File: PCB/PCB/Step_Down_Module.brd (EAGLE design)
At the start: 160 x 100 mm, 22 parts, among them Q1 TPH2900ENH

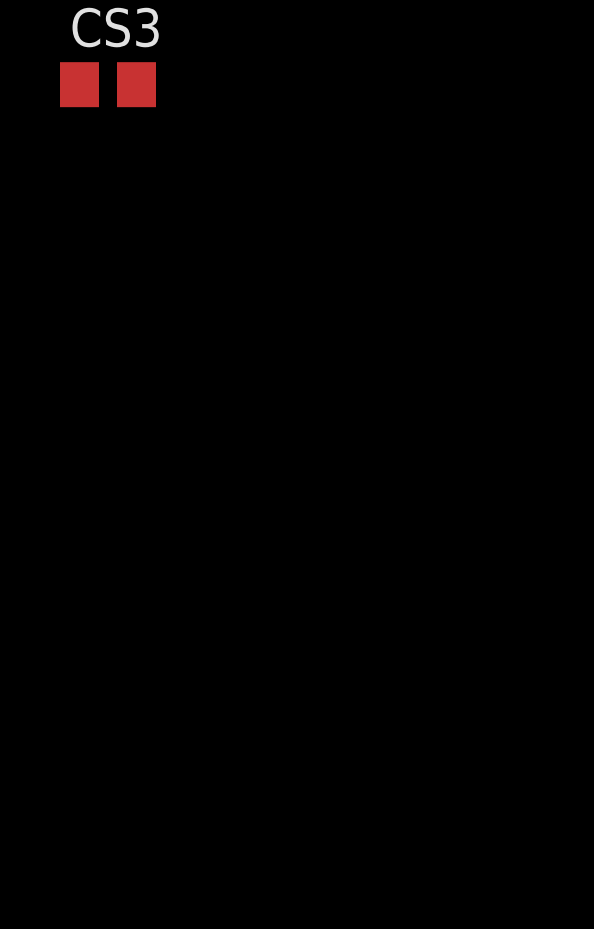
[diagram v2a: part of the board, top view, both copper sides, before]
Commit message: Working on schematic - Added I/O capacitors
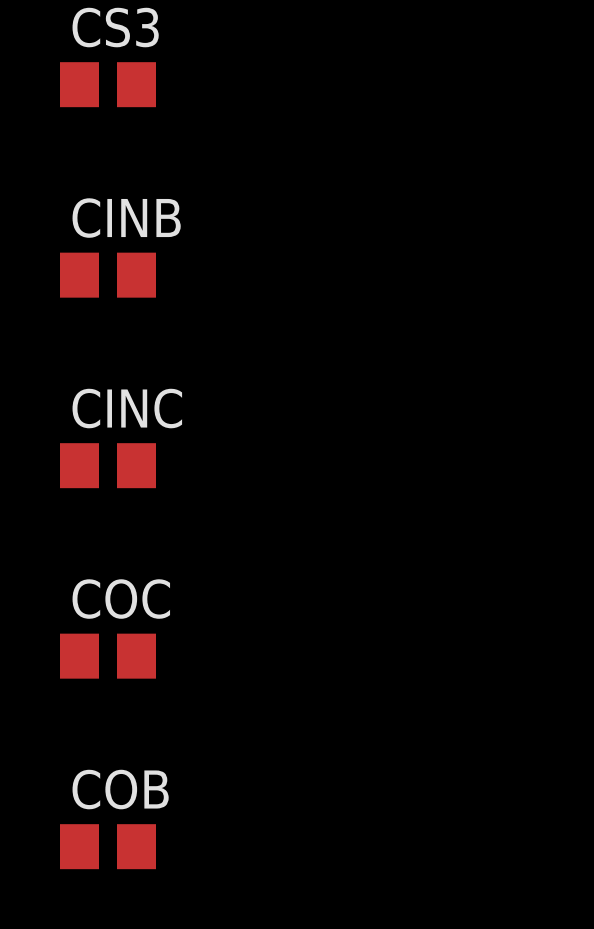
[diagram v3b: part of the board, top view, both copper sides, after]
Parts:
- added CINB: 47uF, rcl:C0805
- added CINC: .47uF, rcl:C0805
- added COB: 150uF, rcl:C0805
- added COC: 22uF, rcl:C0805
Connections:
- removed net N$5: CS.1, CS1.2, RFBT.2, RP.1, U$1.4, U$2.P1
- removed net N$9: U$1.30, U$1.34, U$3.D, U$3.D_1, U$3.D_2, U$3.D_3, U$3.D_4
- new net VIN: CINB.1, CINC.1, U$1.30, U$1.34, U$3.D, U$3.D_1, U$3.D_2, U$3.D_3, U$3.D_4
- new net VOUT: COB.1, COC.1, CS.1, CS1.2, RFBT.2, RP.1, U$1.4, U$2.P1
- net GND: now also CINB.2, CINC.2, COB.2, COC.2
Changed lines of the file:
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@@
 <attribute name="SPICEPREFIX" value="C" x="-35.56" y="-109.22" size="1.778" layer="27" display="off"/>
+</element>
+<element name="CINB" library="rcl" library_urn="urn:adsk.eagle:library:334" package="C0805" package3d_urn="urn:adsk.eagle:package:23617/2" value="47uF" x="-35.56" y="-115.57">
+<attribute name="SPICEPREFIX" value="C" x="-35.56" y="-115.57" size="1.778" layer="27" display="off"/>
+</element>
+<element name="CINC" library="rcl" library_urn="urn:adsk.eagle:library:334" package="C0805" package3d_urn="urn:adsk.eagle:package:23617/2" value=".47uF" x="-35.56" y="-121.92">
+<attribute name="SPICEPREFIX" value="C" x="-35.56" y="-121.92" size="1.778" layer="27" display="off"/>
+</element>
+<element name="COC" library="rcl" library_urn="urn:adsk.eagle:library:334" package="C0805" package3d_urn="urn:adsk.eagle:package:23617/2" value="22uF" x="-35.56" y="-128.27">
+<attribute name="SPICEPREFIX" value="C" x="-35.56" y="-128.27" size="1.778" layer="27" display="off"/>
+</element>
+<element name="COB" library="rcl" library_urn="urn:adsk.eagle:library:334" package="C0805" package3d_urn="urn:adsk.eagle:package:23617/2" value="150uF" x="-35.56" y="-134.62">
+<attribute name="SPICEPREFIX" value="C" x="-35.56" y="-134.62" size="1.778" layer="27" display="off"/>
 </element>
 </elements>
@@
 <wire x1="-36.51" y1="-6.35" x2="25.345" y2="28.48" width="0" layer="19" extent="1-1"/>
 </signal>
-<signal name="N$5">
+<signal name="VOUT">
 <contactref element="U$2" pad="P1"/>
 <contactref element="U$1" pad="4"/>
@@
 <contactref element="RFBT" pad="2"/>
 <contactref element="CS1" pad="2"/>
+<contactref element="COC" pad="1"/>
+<contactref element="COB" pad="1"/>
+<wire x1="-36.51" y1="-128.27" x2="-36.51" y2="-134.62" width="0" layer="19" extent="1-1"/>
+<wire x1="-34.61" y1="-39.37" x2="-36.51" y2="-128.27" width="0" layer="19" extent="1-1"/>
 <wire x1="-34.61" y1="-27.94" x2="-34.61" y2="-39.37" width="0" layer="19" extent="1-1"/>
 <wire x1="-36.51" y1="-21.59" x2="-34.61" y2="-27.94" width="0" layer="19" extent="1-1"/>
@@
 <wire x1="19.795" y1="33.98" x2="-36.51" y2="-27.94" width="0" layer="19" extent="1-1"/>
 </signal>
-<signal name="N$9">
+<signal name="VIN">
 <contactref element="U$1" pad="30"/>
 <contactref element="U$1" pad="34"/>
@@
 <contactref element="U$3" pad="D_1"/>
 <contactref element="U$3" pad="D_3"/>
-<wire x1="25.345" y1="32.48" x2="25.345" y2="34.48" width="0" layer="19" extent="1-1"/>
-<wire x1="-25.695" y1="-1.015" x2="25.345" y2="32.48" width="0" layer="19" extent="1-1"/>
-<wire x1="-26.345" y1="-1.015" x2="-25.695" y2="-1.015" width="0" layer="19" extent="1-1"/>
+<contactref element="CINB" pad="1"/>
+<contactref element="CINC" pad="1"/>
+<wire x1="-36.51" y1="-115.57" x2="-36.51" y2="-121.92" width="0" layer="19" extent="1-1"/>
+<wire x1="-26.67" y1="-2.09" x2="-36.51" y2="-115.57" width="0" layer="19" extent="1-1"/>
+<wire x1="-26.345" y1="-1.015" x2="-26.67" y2="-2.09" width="0" layer="19" extent="1-1"/>
+<wire x1="-25.695" y1="-1.015" x2="-26.345" y2="-1.015" width="0" layer="19" extent="1-1"/>
 <wire x1="-26.995" y1="-1.015" x2="-26.345" y2="-1.015" width="0" layer="19" extent="1-1"/>
 <wire x1="-27.645" y1="-1.015" x2="-26.995" y2="-1.015" width="0" layer="19" extent="1-1"/>
-<wire x1="-26.67" y1="-2.09" x2="-26.345" y2="-1.015" width="0" layer="19" extent="1-1"/>
+<wire x1="25.345" y1="32.48" x2="-25.695" y2="-1.015" width="0" layer="19" extent="1-1"/>
+<wire x1="25.345" y1="34.48" x2="25.345" y2="32.48" width="0" layer="19" extent="1-1"/>
 </signal>
 <signal name="N$10">
@@
 <contactref element="U$1" pad="36"/>
 <contactref element="CS3" pad="2"/>
+<contactref element="CINB" pad="2"/>
+<contactref element="CINC" pad="2"/>
+<contactref element="COC" pad="2"/>
+<contactref element="COB" pad="2"/>
+<wire x1="-34.61" y1="-128.27" x2="-34.61" y2="-134.62" width="0" layer="19" extent="1-1"/>
+<wire x1="-34.61" y1="-121.92" x2="-34.61" y2="-128.27" width="0" layer="19" extent="1-1"/>
+<wire x1="-34.61" y1="-115.57" x2="-34.61" y2="-121.92" width="0" layer="19" extent="1-1"/>
+<wire x1="-34.61" y1="-109.22" x2="-34.61" y2="-115.57" width="0" layer="19" extent="1-1"/>
 <wire x1="-36.51" y1="-83.82" x2="-34.61" y2="-109.22" width="0" layer="19" extent="1-1"/>
 <wire x1="-36.51" y1="-77.47" x2="-36.51" y2="-83.82" width="0" layer="19" extent="1-1"/>

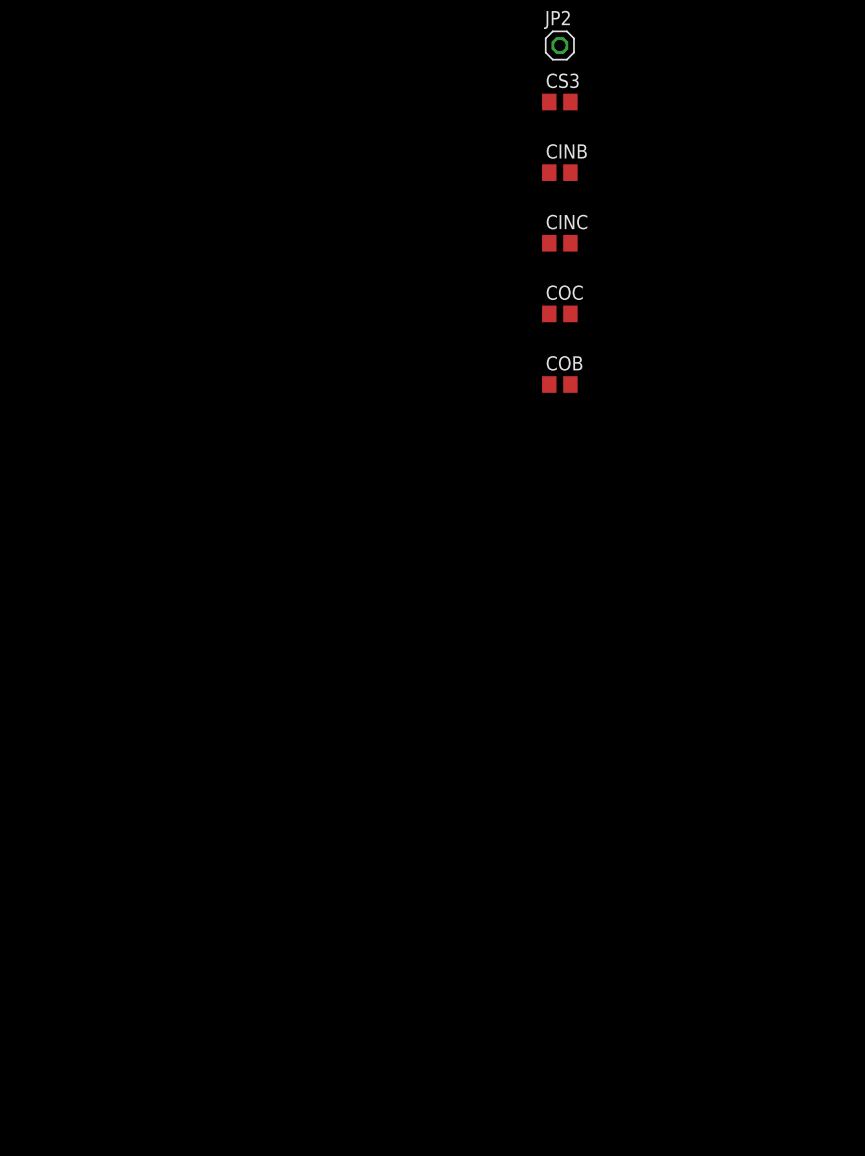
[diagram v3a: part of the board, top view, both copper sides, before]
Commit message: Working on schematic - Added DRVCC transistor, made a lot of changes to the pin state
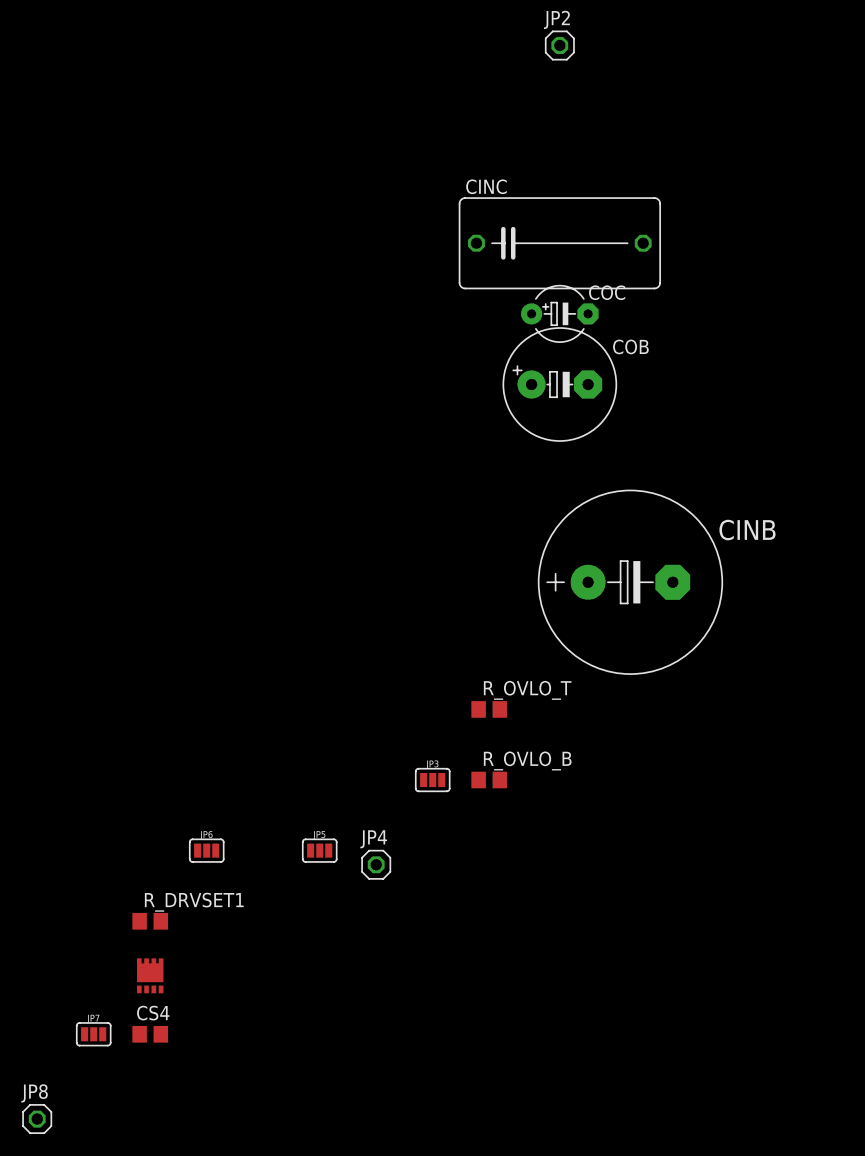
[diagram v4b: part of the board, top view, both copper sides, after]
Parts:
- removed CS3: 4.7uF, rcl:C0805
- added CS4: 4.7uF, rcl:C0805
- added JP3, JP5, JP6, JP7: JUMPER-SMT_3_1-NC_PASTE_SILK, SparkFun-Jumpers:SMT-JUMPER_3_1-NC_PASTE_SILK
- added JP4, JP8: (no value), pinhead:1X01
- added R_DRVSET1: 80.6k, rcl:R0805
- added R_OVLO_B: 1k, rcl:R0805
- added R_OVLO_T: 124k, rcl:R0805
- added U$4: FDMC86240, Switching_MOS:8-MLP/POWERWFDN
- CINB: device rcl:C0805 -> rcl:E7,5-16
- CINC: device rcl:C0805 -> rcl:C150-084X183
- COB: device rcl:C0805 -> rcl:E5-10,5
- COC: device rcl:C0805 -> rcl:E5-5
- moved CINB 37.4 mm to (-29.2, -152.4)
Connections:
- removed net N$14: CS3.1, U$1.26, U$1.28
- new net DRVCC: CS4.1, U$1.26, U$4.S_1, U$4.S_2, U$4.S_3
- new net DRVSET: JP6.2, U$1.18
- new net EXTVCC: JP7.2, U$1.32
- new net N$13: JP7.1, JP8.1
- new net N$5: JP6.1, R_DRVSET1.1
- new net N$9: JP3.3, R_OVLO_B.1, R_OVLO_T.2
- new net NDRV: U$1.28, U$4.G
- new net OVLO: JP3.2, U$1.1
- new net PHASEMD: JP5.2, U$1.36
- new net PLLIN: JP4.1, U$1.13
- net GND: now also CINB.-, COB.-, COC.-, CS4.2, JP3.1, JP5.1, JP7.3, R_DRVSET1.2, R_OVLO_B.2, U$1.19, U$1.37; no longer CINB.2, COB.2, COC.2, CS3.2, U$1.1, U$1.36, U$1.8
- net INTVCC: now also JP5.3, JP6.3, U$1.8; no longer U$1.19
- net VIN: now also CINB.+, R_OVLO_T.1, U$4.D, U$4.D_1, U$4.D_2, U$4.D_3, U$4.D_4; no longer CINB.1
- net VOUT: now also COB.+, COC.+; no longer COB.1, COC.1

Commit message: Removed folder: Adithya
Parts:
- removed C1: 0.1uF, rcl:C0805
- added CINC1: .47uF, rcl:C150-084X183
- added COB1: 150uF, rcl:E5-10,5
- added COC1: 22uF, rcl:E5-5
- added POT_FB: 10k, rcl:RTRIM64W
- added RS2: 10k, rcl:R0805
- RFBB: value 10k -> 4.7k
- RFBT: value 390k -> 180k
- RS: value 280K -> 270k
- R_OVLO_T: value 124k -> 120k
- moved JP7 269.7 mm to (66.9, 34.8), turned to 90 degrees
- moved JP8 262.9 mm to (66.9, 15.6)
- moved R_DRVSET1 244.8 mm to (57.3, 24.7), turned to 90 degrees
- moved R_OVLO_B 236.1 mm to (53.5, 45.8), turned to 180 degrees
- moved JP3 235.9 mm to (53.6, 43.2)
- moved JP6 234.1 mm to (54.0, 23.7), turned to 180 degrees
- moved R_OVLO_T 232.1 mm to (57.7, 45.8), turned to 180 degrees
- moved JP4 221.0 mm to (54.7, 15.6)
- moved RS1 153.0 mm to (49.5, 30.6), turned to 90 degrees
- moved JP2 148.0 mm to (51.6, 15.5), turned to 90 degrees
- moved C2 140.9 mm to (46.7, 30.6), turned to 90 degrees
- moved JP1 135.8 mm to (48.4, 15.4), turned to 90 degrees
- moved RFREQ 133.0 mm to (49.5, 24.8), turned to 90 degrees
- moved CS5 128.3 mm to (42.5, 30.6), turned to 270 degrees
- moved RTH 115.3 mm to (39.4, 22.9), turned to 180 degrees
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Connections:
- net N$10 renamed ITH
- net N$7 renamed SS
- new net N$14: CS1.2, POT_FB.2, RFBT.2
- new net N$7: RS.1, RS2.2
- net GND: now also COB1.-, COC1.-, POT_FB.3
- net N$3: now also CINC1.2; no longer C1.2
- net N$4: now also CINC1.1; no longer C1.1
- net N$6: now also RS2.1; no longer RS.1
- net VOUT: now also COB1.+, COC1.+, POT_FB.1; no longer CS1.2, RFBT.2
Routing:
- net INTVCC: track 0.00 -> 45.8 mm, vias 0 -> 4
- net VOUT: track 0.00 -> 29.2 mm
- net N$8: track 0.00 -> 28.2 mm
- net ITH: track 0.00 -> 26.1 mm, vias 0 -> 2
- net PGOOD: track 0.00 -> 21.2 mm, vias 0 -> 1
- net CLKOUT: track 0.00 -> 20.3 mm, vias 0 -> 1
- net N$13: track 0.00 -> 18.4 mm
- net PLLIN: track 0.00 -> 18.0 mm, vias 0 -> 1
- net SS: track 0.00 -> 16.7 mm, vias 0 -> 2
- net N$14: track 0.00 -> 11.9 mm
- net N$6: track 0.00 -> 11.8 mm
- net N$11: track 0.00 -> 7.50 mm
- net OVLO: track 0.00 -> 6.76 mm
- net DRVSET: track 0.00 -> 6.56 mm
- net EXTVCC: track 0.00 -> 6.04 mm
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
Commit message: Initial routing of PCB with design considerations
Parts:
- removed POT_FB: 10k, rcl:RTRIM64W
- removed U$2: PQ2614BLA, Inductors:PQ2614BLA
- added L1: PQ2614BLA, Inductors:PQ2614BLA
- added U$5, U$7: IO_PAD, IO_pad:IO_DOUBLE
- added V_ADJ: 10k, pot:RM065
- moved CINC1 213.5 mm to (17.7, 69.3), turned to 90 degrees
- moved CS4 173.2 mm to (20.6, 56.9)
- moved U$4 159.0 mm to (13.8, 49.4), turned to 90 degrees
- moved COC1 152.7 mm to (-17.9, 36.6), turned to 180 degrees
- moved COB1 142.5 mm to (-17.7, 17.0), turned to 180 degrees
- moved JP5 133.3 mm to (26.0, 32.1), flipped to the bottom, turned to 180 degrees
- moved CINB 122.3 mm to (1.02, 67.9), turned to 180 degrees
- moved CINC 107.6 mm to (1.02, 81.7), turned to 180 degrees
- moved COC 72.6 mm to (-17.9, 42.7), turned to 180 degrees
- moved U$3 68.0 mm to (8.13, 55.9)
- moved COB 66.8 mm to (-17.8, 27.8), turned to 180 degrees
- moved Q1 63.0 mm to (-0.51, 54.0)
- moved R_OVLO_T 57.6 mm to (21.5, 90.7), turned to 270 degrees
- moved JP3 54.5 mm to (18.7, 85.0), turned to 90 degrees
- moved CTH 53.7 mm to (26.9, 76.2), turned to 90 degrees
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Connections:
- net GND: now also U$5.NEG, U$5.NEG_1, U$5.NEG_10, U$5.NEG_11, U$5.NEG_12, U$5.NEG_13, U$5.NEG_14, U$5.NEG_15, U$5.NEG_16, U$5.NEG_17, U$5.NEG_18, U$5.NEG_19, U$5.NEG_2, U$5.NEG_20, U$5.NEG_3, U$5.NEG_4, U$5.NEG_5, U$5.NEG_6, U$5.NEG_7, U$5.NEG_8, U$5.NEG_9, U$7.NEG, U$7.NEG_1, U$7.NEG_10, U$7.NEG_11, U$7.NEG_12, U$7.NEG_13, U$7.NEG_14, U$7.NEG_15, U$7.NEG_16, U$7.NEG_17, U$7.NEG_18, U$7.NEG_19, U$7.NEG_2, U$7.NEG_20, U$7.NEG_3, U$7.NEG_4, U$7.NEG_5, U$7.NEG_6, U$7.NEG_7, U$7.NEG_8, U$7.NEG_9, V_ADJ.E; no longer POT_FB.3
- net N$14: now also V_ADJ.S; no longer CS1.2, POT_FB.2
- net N$3: now also L1.P2; no longer U$2.P2
- net VIN: now also U$5.POS, U$5.POS_1, U$5.POS_10, U$5.POS_11, U$5.POS_12, U$5.POS_13, U$5.POS_14, U$5.POS_15, U$5.POS_16, U$5.POS_17, U$5.POS_18, U$5.POS_19, U$5.POS_2, U$5.POS_20, U$5.POS_3, U$5.POS_4, U$5.POS_5, U$5.POS_6, U$5.POS_7, U$5.POS_8, U$5.POS_9
- net VOUT: now also CS1.2, L1.P1, U$7.POS, U$7.POS_1, U$7.POS_10, U$7.POS_11, U$7.POS_12, U$7.POS_13, U$7.POS_14, U$7.POS_15, U$7.POS_16, U$7.POS_17, U$7.POS_18, U$7.POS_19, U$7.POS_2, U$7.POS_20, U$7.POS_3, U$7.POS_4, U$7.POS_5, U$7.POS_6, U$7.POS_7, U$7.POS_8, U$7.POS_9, V_ADJ.A; no longer POT_FB.1, U$2.P1
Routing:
- net GND: track 3.68 -> 522.7 mm
- net VOUT: track 29.2 -> 181.0 mm
- net N$3: track 0.00 -> 99.7 mm, vias 0 -> 1
- net VIN: track 0.00 -> 98.8 mm, vias 0 -> 2
- net OVLO: track 6.76 -> 48.8 mm, vias 0 -> 2
- net PHASEMD: track 0.00 -> 20.9 mm, vias 0 -> 1
- net CLKOUT: track 20.3 -> 0.00 mm, vias 1 -> 0
- net N$13: track 18.4 -> 0.00 mm
- net PLLIN: track 18.0 -> 0.00 mm, vias 1 -> 0
- net EXTVCC: track 6.04 -> 22.0 mm, vias 0 -> 1
- net N$2: track 0.00 -> 15.1 mm, vias 0 -> 2
- net DRVCC: track 0.00 -> 14.4 mm, vias 0 -> 2
- net N$8: track 28.2 -> 16.4 mm
- net ITH: track 26.1 -> 37.2 mm
- net N$4: track 0.00 -> 10.6 mm, vias 0 -> 1
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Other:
- board size 160 x 100 mm -> 191.8 x 104.1 mm

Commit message: Finalized PCB - first iteration
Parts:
- moved CINC1 32.5 mm to (50.0, 66.4)
- moved R_OVLO_B 32.2 mm to (53.2, 79.8)
- moved R_OVLO_T 32.2 mm to (53.2, 85.3)
- moved JP3 32.2 mm to (50.4, 79.6)
- moved RS2 32.1 mm to (52.0, 36.4)
- moved RS 32.1 mm to (52.0, 40.7)
- moved U$5 32.0 mm to (33.0, 87.6)
- moved CINC 31.9 mm to (32.8, 79.1)
- moved CINB 31.8 mm to (32.8, 66.7)
- moved COB 31.8 mm to (14.0, 29.1)
- moved COB1 31.8 mm to (14.1, 18.3)
- moved COC 31.8 mm to (13.8, 43.9)
- moved COC1 31.8 mm to (13.8, 37.8)
- moved L1 31.8 mm to (34.3, 28.7)
- moved U$3 31.8 mm to (39.9, 54.6)
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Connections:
- net GND: now also U$1.39_B; no longer U$1.PWR_PAD16, U$1.PWR_PAD17, U$1.PWR_PAD18
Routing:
- net GND: track 522.7 -> 603.6 mm
- net CLKOUT: track 0.00 -> 25.1 mm, vias 0 -> 1
- net PLLIN: track 0.00 -> 21.3 mm, vias 0 -> 1
- net N$3: track 99.7 -> 92.4 mm
- net N$13: track 0.00 -> 4.83 mm
- net ITH: track 37.2 -> 41.8 mm
- net OVLO: track 48.8 -> 45.6 mm
- net VOUT: track 181.0 -> 178.9 mm
- net VIN: track 98.8 -> 97.7 mm
- net INTVCC: track 49.2 -> 50.2 mm
- net N$8: track 16.4 -> 15.4 mm
- net N$1: track 8.83 -> 8.12 mm
- net N$4: track 10.6 -> 9.91 mm
- net N$6: track 14.2 -> 13.5 mm
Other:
- board size 191.8 x 104.1 mm -> 68 x 99.2 mm
- board text added: "140-30V"
- board text added: "ATLAS"
- board text added: "Step Down"
- board text added: "v1"
